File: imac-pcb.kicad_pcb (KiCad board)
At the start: 2 copper layers, 90 x 60 mm, 73 parts, among them J1 EXT_IN, J2 STEREO_OUT, P1 PROBE1, P2 PATCHBAY_IO, P3 PROBE2, P4 EXT_OUT, P5 INPUTS, P6 PATCHBAY_A, P7 PWR_X3, Q1 NX3008N***, Q2 PMV48XP, Q3 NX3008N***, Q4 NX3008N***, SW1 RESET_SW, U1 MCP6004, U2 MCP6002, U3 NCP4620, U4 ADG849, U5 arduino_pro_micro, U6 NCP1117-5

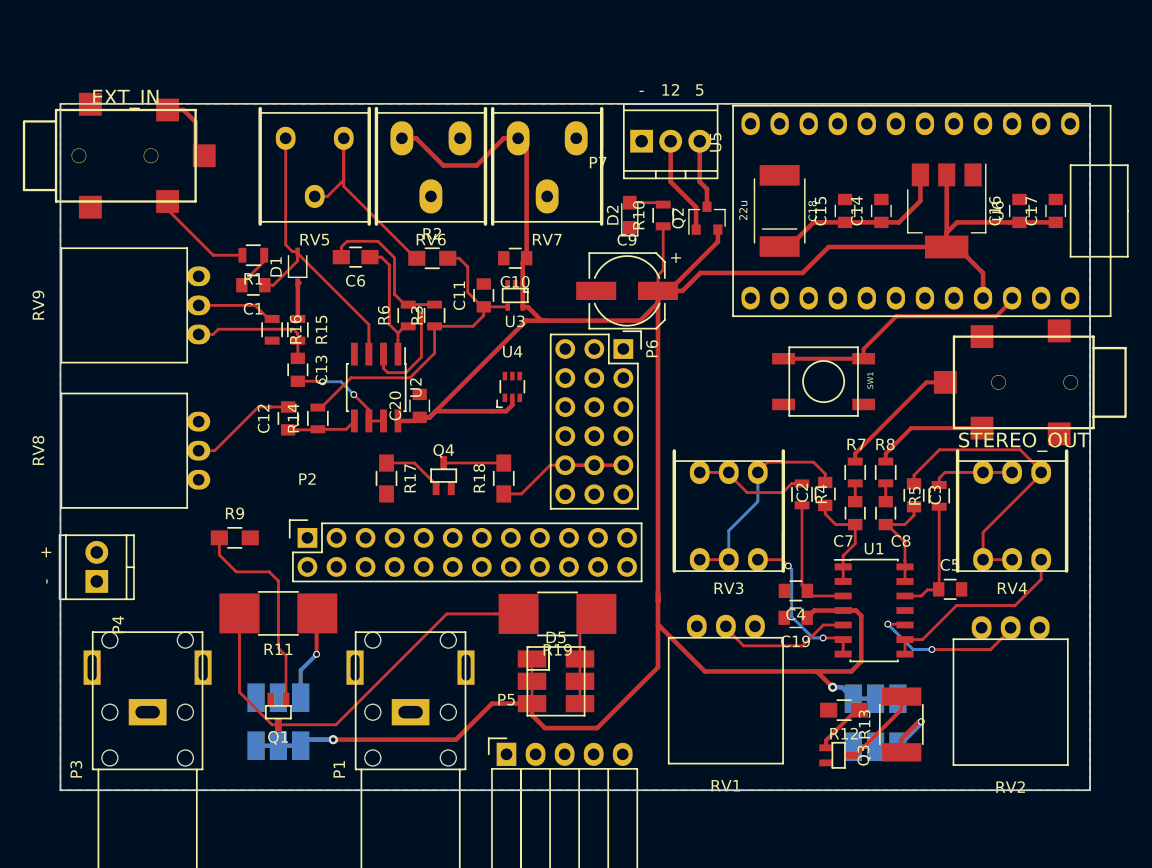
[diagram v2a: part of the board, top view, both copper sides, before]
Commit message: finished routing & moving references in silkscreen
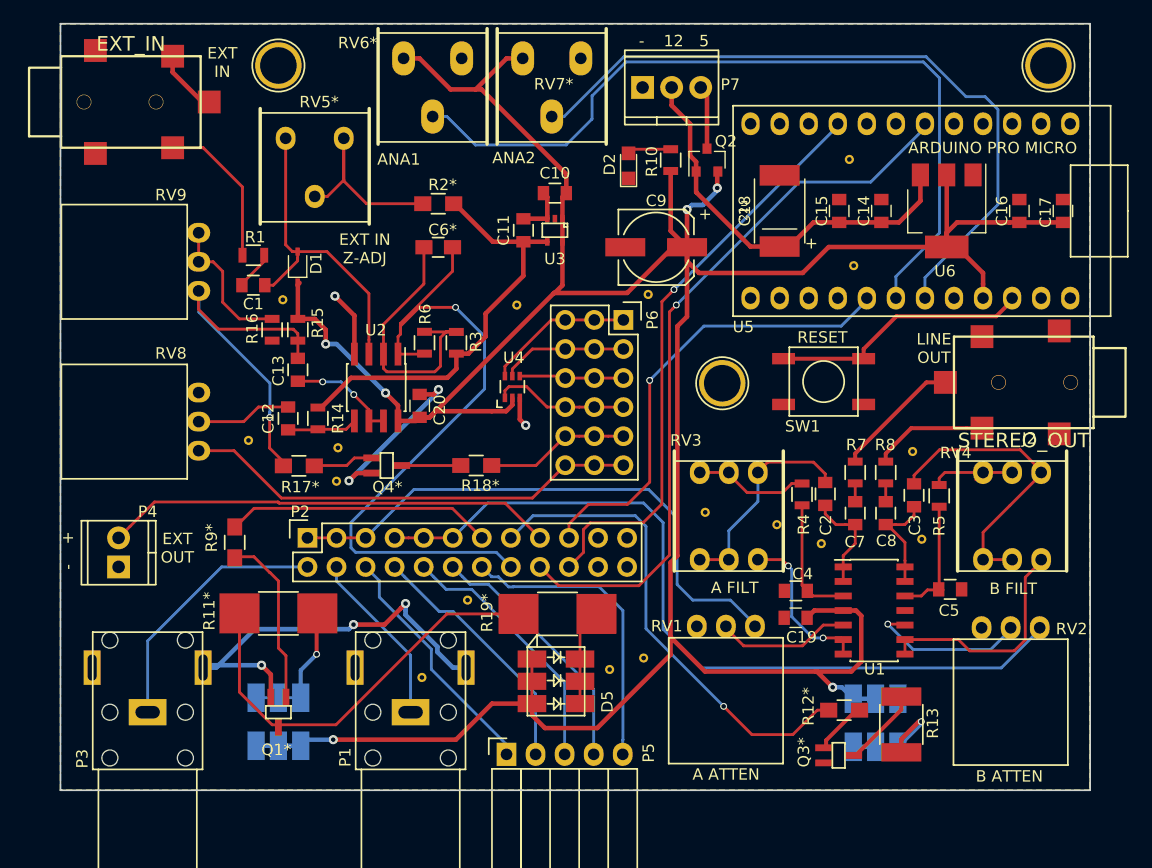
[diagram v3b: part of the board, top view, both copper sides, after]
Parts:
- added REF**: via-0.6mm, imac:via-0.4mm, F.Cu at (24.3, 20.1)
- added REF**: via-0.6mm, imac:via-0.4mm, F.Cu at (19.4, 7.12)
- added REF**: via-0.6mm, imac:via-0.4mm, F.Cu at (39.9, 7.59)
- added REF**: via-0.6mm, imac:via-0.4mm, F.Cu at (16.4, 19.4)
- added REF**: via-0.6mm, imac:via-0.4mm, F.Cu at (69.0, -5.14)
- added REF**: via-0.6mm, imac:via-0.4mm, F.Cu at (31.6, 40.1)
- added REF**: 1pin, Connectors:1pin, F.Cu at (19.1, -13.4)
- added REF**: 1pin, Connectors:1pin, F.Cu at (86.4, -13.4)
- added REF**: 1pin, Connectors:1pin, F.Cu at (57.8, 14.4)
- added REF**: via-0.6mm, imac:via-0.4mm, F.Cu at (35.6, 33.4)
- added REF**: via-0.6mm, imac:via-0.4mm, F.Cu at (48.0, 39.4)
- added REF**: via-0.6mm, imac:via-0.4mm, F.Cu at (24.1, 23.0)
- added REF**: via-0.6mm, imac:via-0.4mm, F.Cu at (51.0, 38.4)
- added REF**: via-0.6mm, imac:via-0.4mm, F.Cu at (51.4, 6.66)
- added REF**: via-0.6mm, imac:via-0.4mm, F.Cu at (69.3, 4.15)
- added REF**: via-0.6mm, imac:via-0.4mm, F.Cu at (74.5, 20.4)
- added REF**: via-0.6mm, imac:via-0.4mm, F.Cu at (75.3, 28.1)
- added REF**: via-0.6mm, imac:via-0.4mm, F.Cu at (62.6, 26.8)
- added REF**: via-0.6mm, imac:via-0.4mm, F.Cu at (66.5, 28.4)
- added REF**: via-0.6mm, imac:via-0.4mm, F.Cu at (56.4, 25.7)
- D3, D4, D5: footprint Imac:PLCC6-3in1-SMD-LED -> imac:PLCC6-3in1-SMD-LED
- moved R17* 7.74 mm to (20.8, 21.6), turned to 180 degrees
- moved C6* 7.27 mm to (33.0, 2.54)
- moved RV7* 7.00 mm to (42.9, -11.4)
- moved RV6* 6.99 mm to (32.5, -11.4)
- moved C10 6.67 mm to (43.2, -2.19)
- moved C11 6.67 mm to (40.5, 1.06)
- moved U3 6.67 mm to (43.2, 1.06)
- moved Q2 5.08 mm to (56.5, -5.08)
- moved Q4* 5.06 mm to (28.5, 21.6), turned to 270 degrees
- moved R10 4.88 mm to (53.3, -5.08)
- moved R2* 4.80 mm to (33.0, -1.27)
- moved J1 4.72 mm to (6.15, -10.2)
- moved P7 4.70 mm to (50.9, -11.4)
- moved C9 4.58 mm to (52.1, 2.54)
- moved D2 4.31 mm to (49.7, -4.57)
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- renumbered C6 to C6*, Q1 to Q1*, Q3 to Q3*, Q4 to Q4*, R11 to R11*, R12 to R12*, R17 to R17*, R18 to R18*, R19 to R19*, R2 to R2*, R9 to R9*, RV5 to RV5*, RV6 to RV6*, RV7 to RV7*
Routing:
- net /A1_IN: track 0.00 -> 70.9 mm
- net /AUDIOB_SEND: track 0.00 -> 70.6 mm
- net GND: track 5.83 -> 70.0 mm, vias 0 -> 7
- net /D3: track 0.00 -> 63.8 mm, vias 0 -> 1
- net /A2_IN: track 0.00 -> 62.9 mm
- net /D6: track 0.00 -> 51.2 mm, vias 0 -> 1
- net /EXT_IN: track 11.2 -> 61.7 mm, vias 0 -> 1
- net /AUDIOA_SEND: track 0.00 -> 49.3 mm
- net /LED_CTRL2: track 0.00 -> 42.6 mm, vias 0 -> 1
- net /A0_IN: track 0.00 -> 40.8 mm, vias 0 -> 1
- net /MOD_CTRL: track 0.00 -> 40.0 mm
- net /EXT_OUT: track 0.00 -> 39.4 mm
- net /IN5: track 0.00 -> 26.5 mm
- net 5V_SYS: track 250.7 -> 275.9 mm, vias 2 -> 6
- net /LED_CTRL1: track 0.00 -> 23.6 mm
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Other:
- board size 90 x 60 mm -> 90 x 67 mm
- board text added: "+"
- board text added: "A ATTEN"
- board text added: "A FILT"
- board text added: "ANA1"
- board text added: "ANA2"
- board text added: "ARDUINO PRO MICRO"
- board text added: "B ATTEN"
- board text added: "B FILT"
- board text added: "EXT IN"
- board text added: "EXT IN Z-ADJ"
- board text added: "EXT OUT"
- board text added: "LINE OUT"
- board text added: "RESET"
- board text removed: "TODO: - make a hand solderable version of the SOIC14 chip - make a hand solderable mosfet version"

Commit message: final schematic for run v01
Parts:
- added G***: LOGO, imac:kare-warning, B.Cu at (170.9, 123.9)
- added REF**: via-0.6mm, imac:via-0.4mm, F.Cu at (165.5, 88.3)
- moved Q3* 144.7 mm to (173.1, 146.4), turned to 0 degrees
- moved R12* 143.5 mm to (167.9, 146.5), turned to 90 degrees
- moved C1 141.4 mm to (116.9, 105.9)
- moved C12 141.4 mm to (119.9, 117.5)
- moved C13 141.4 mm to (120.8, 113.2)
- moved C14 141.4 mm to (171.8, 99.4)
- moved C15 141.4 mm to (168.1, 99.4)
- moved C16 141.4 mm to (183.8, 99.4)
- moved C17 141.4 mm to (187.6, 99.4)
- moved C18 141.4 mm to (162.9, 99.4)
- moved C19 141.4 mm to (164.3, 134.9)
- moved C2 141.4 mm to (166.8, 124.1)
- moved C20 141.4 mm to (131.4, 116.4)
- moved C3 141.4 mm to (174.6, 124.2)
- moved C4 141.4 mm to (164.3, 132.6)
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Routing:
- net 5V_SYS: track 275.9 -> 280.9 mm
- net Net-(Q3-Pad3): track 7.18 -> 5.34 mm
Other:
- board text added: "1"
- board text added: "2"
- board text added: "3"
- board text added: "4"
- board text added: "5"
- board text added: "A ATTENUATE"
- board text added: "A FILTER CUTOFF"
- board text added: "A0"
- board text added: "AUDIO_A"
- board text added: "AUDIO_B"
- board text added: "B ATTENUATE"
- board text added: "B FILTER CUTOFF"
- board text added: "D3"
- board text added: "D6"
- board text added: "EXTin"
- board text added: "EXTout"
- board text added: "GND"
- board text added: "IN"
- board text added: "IN1"
- board text added: "IN2"
- board text added: "IN3"
- board text added: "IN4"
- board text added: "IN5"
- board text added: "L1"
- board text added: "L2"
- board text added: "Please drive carefully"
- board text added: "backseat driver v01 2016 j.reus"
- board text added: "mod ATTEN"
- board text added: "mod BIAS"
- board text added: "modCTL"
- board text added: "modIN"
- board text added: "swCOM"
- board text added: "swCTL"
- board text added: "swNC"
- board text added: "swNO"
- board text removed: "A ATTEN"
- board text removed: "A FILT"
- board text removed: "B ATTEN"
- board text removed: "B FILT"
